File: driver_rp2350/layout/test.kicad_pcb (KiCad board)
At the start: 6 copper layers, 45 x 45 mm, 463 parts, among them J1 Conn_01x04, J2 Conn_01x05, J3 Conn_01x05, J4 Conn_01x05, J5 Conn_01x05, SW1 SW_Push, SW2 SW_Push, U1 APS6404L-3SQR, U10 UCC27517, U11 UCC27517, U12 UCC27517, U13 UCC27517, U14 UCC27517, U15 UCC27517, U16 UCC27517, U17 UCC27517, U18 UCC27517, U19 UCC27517, U2 RP2354B_80QFN, U20 UCC27517, U21 UCC27517, U22 UCC27517, U23 UCC27517, U24 UCC27517, U25 UCC27517, U26 UCC27517, U27 UCC27517, U28 UCC27517, U29 UCC27517, U3 UCC27517, U30 UCC27517, U31 UCC27517, U32 UCC27517, U33 UCC27517, U34 UCC27517, U35 UCC27517, U36 UCC27517, U37 UCC27517, U38 UCC27517, U39 AP2112K-3.3, U4 UCC27517, U5 UCC27517, U6 UCC27517, U7 UCC27517, U8 UCC27517, U9 UCC27517, Y1 ABM8-272-T3

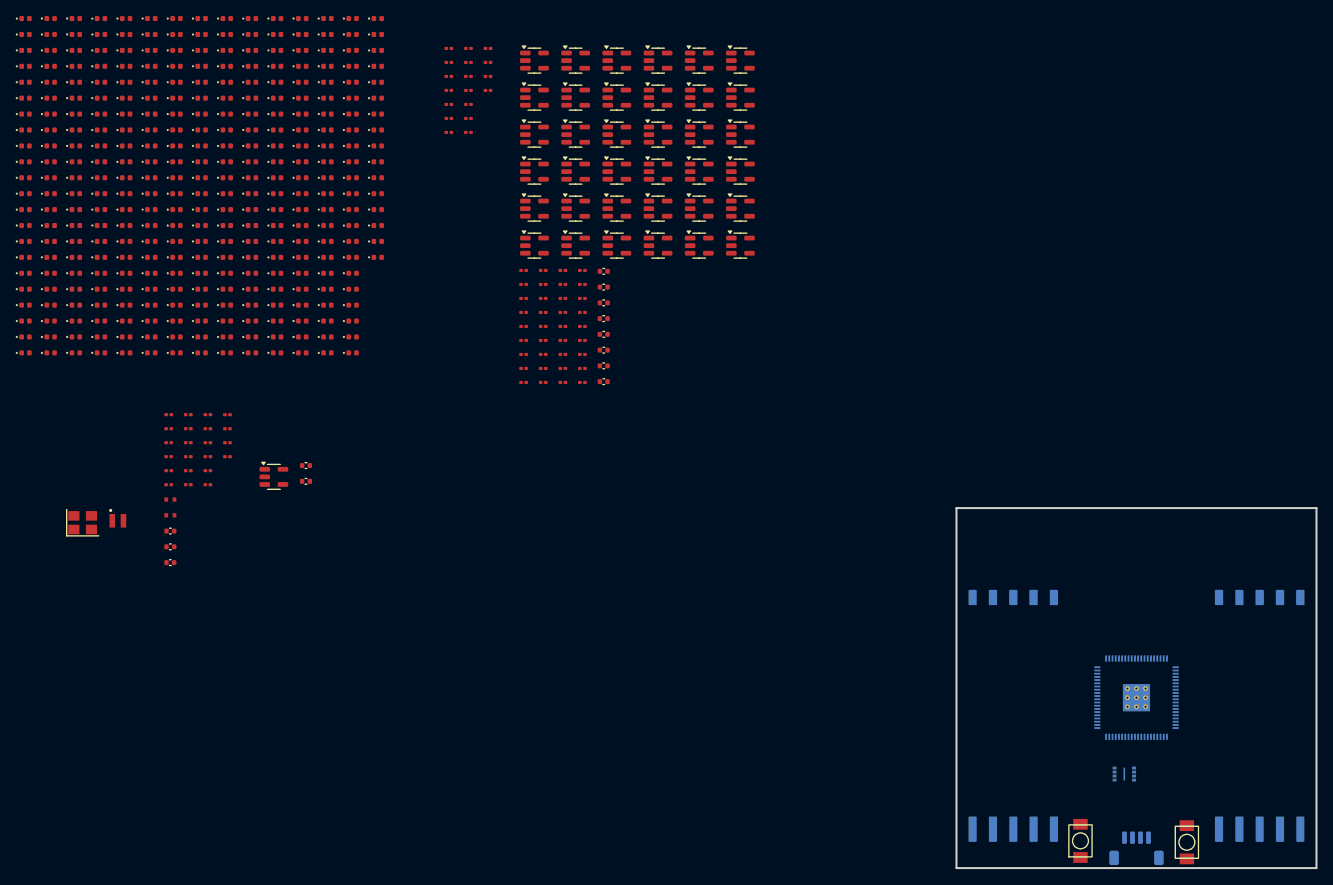
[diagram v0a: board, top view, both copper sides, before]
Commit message: Worked on multi-color led layout.
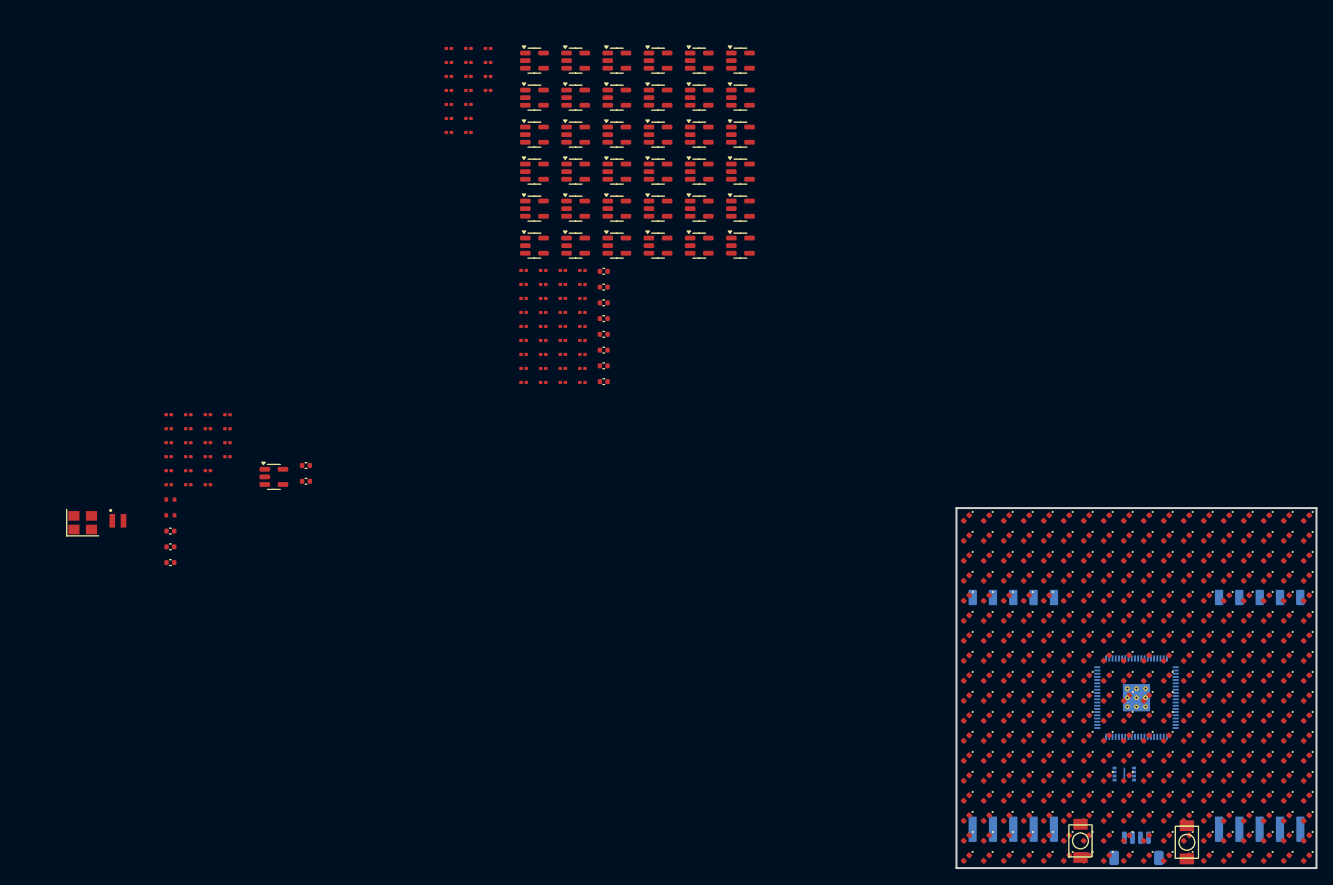
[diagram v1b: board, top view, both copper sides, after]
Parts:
- moved D69 177.3 mm to (93.8, 86.2), turned to -135 degrees
- moved D52 176.2 mm to (93.8, 88.8), turned to -135 degrees
- moved D35 175.5 mm to (93.8, 91.2), turned to -135 degrees
- moved D18 175.2 mm to (93.8, 93.8), turned to -135 degrees
- moved D68 174.9 mm to (91.2, 83.8), turned to -135 degrees
- moved D51 173.8 mm to (91.2, 86.2), turned to -135 degrees
- moved D34 173.1 mm to (91.2, 88.8), turned to -135 degrees
- moved D17 172.7 mm to (91.2, 91.2), turned to -135 degrees
- moved D67 172.5 mm to (88.8, 81.2), turned to -135 degrees
- moved D50 171.4 mm to (88.8, 83.8), turned to -135 degrees
- moved D33 170.6 mm to (88.8, 86.2), turned to -135 degrees
- moved D16 170.2 mm to (88.8, 88.8), turned to -135 degrees
- moved D49 169.0 mm to (86.2, 81.2), turned to -135 degrees
- moved D32 168.2 mm to (86.2, 83.8), turned to -135 degrees
- moved D15 167.7 mm to (86.2, 86.2), turned to -135 degrees
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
